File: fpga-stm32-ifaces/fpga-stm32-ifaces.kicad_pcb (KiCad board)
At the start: 6 copper layers, 90 x 94.5 mm, 274 parts, among them J1 0826-1G1T-23-F, J10 CORTEX_DEBUG_ETM, J11 XILINX_JTAG, J12 CONN_01X03, J2 PMOD_HOST, J3 PMOD_HOST, J4 XILINX_JTAG, J5 CONN_01X03, J6 CONN_01X03, J7 CONN_PCIE_PWR_8PIN, J8 XILINX_JTAG, J9 CONN_IBC_MGMT_DEVICE, M1 LOGO, M2 LOGO, M3 LOGO, M5 SCREWHOLE, M6 SCREWHOLE, M7 SCREWHOLE, M8 SCREWHOLE, U1 STM32H735-UFBGA176-25, U10 ECS-1612MV-250-CN, U11 STM32L431-QFN48, U12 MUN12AD03-SE, U13 MUN12AD03-SE, U14 MUN12AD03-SE, U15 MUN12AD03-SE, U16 W25Q128JV, U2 XC7S25-1FTGB196, U3 S25FL128SAGBHIA10, U4 KSZ9031RN, U5 RCLAMP0514M, U6 RCLAMP0514M, U7 ECS-1612MV-250-CN, U8 AT24MAC402, U9 ECS-1612MV-250-CN

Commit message: Lots of routing cleanup
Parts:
- moved R82 1.77 mm to (82.0, 131.0)
- moved R84 0.50 mm to (81.5, 126.8)
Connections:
- U2 pad B2: /MCU/FPGA_QSPI_DQ7 -> /MCU/FMC_NL_NADV
- U2 pad C1: /MCU/FMC_NL_NADV -> /MCU/FPGA_QSPI_DQ7
- U2 pad J3: /MCU/FMC_AD5 -> /MCU/RMII_RXD1
- U2 pad J4: /MCU/RMII_RXD1 -> /MCU/FMC_AD5
- U2 pad K3: /MCU/FMC_AD9 -> /MCU/RMII_RXD0
- U2 pad K4: /MCU/RMII_CRS_DV -> /MCU/FPGA_QSPI_DQS
- U2 pad L3: /MCU/FPGA_QSPI_DQS -> /MCU/FPGA_QSPI_DQ5
- U2 pad L5: /MCU/FPGA_QSPI_DQ5 -> /MCU/FPGA_QSPI_DQ4
- U2 pad M4: /MCU/RMII_RXD0 -> /MCU/RMII_CRS_DV
- U2 pad M5: /MCU/FPGA_QSPI_DQ4 -> /MCU/FMC_AD9
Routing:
- net /MCU/FMC_NBL1: track 44.1 -> 30.8 mm, vias 4 -> 2
- net /MCU/MCU_JTAG_TDI: track 69.4 -> 75.6 mm, vias 5 -> 4
- net /Power supply/1V0_EN: track 77.9 -> 71.9 mm
- net /MCU/FMC_NOE: track 29.6 -> 23.9 mm
- net /MCU/RMII_CRS_DV: track 31.8 -> 26.6 mm
- net /MCU/FPGA_QSPI_DQ3: track 41.8 -> 36.6 mm
- net /MCU/MCU_UART_RX: track 38.4 -> 33.5 mm
- net /MCU/FPGA_QSPI_DQ2: track 46.5 -> 41.7 mm
- net /Ethernet/ETH_RST_N: track 59.3 -> 63.9 mm, vias 2 -> 0
- net /MCU/RMII_REF_CLK: track 37.4 -> 32.9 mm
- net /MCU/FPGA_QSPI_DQ7: track 25.7 -> 21.4 mm, vias 3 -> 0
- net /MCU/MCU_UART_TX: track 36.0 -> 31.7 mm
- net /MCU/FPGA_QSPI_DQ6: track 21.7 -> 17.6 mm
- net /MCU/MCU_PMOD_DQ3: track 33.3 -> 30.3 mm, vias 3 -> 2
- net /MCU/FPGA_QSPI_DQ5: track 19.3 -> 16.4 mm
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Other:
- board text added: "FPGA-STM32H7 Interface Test A. Zonenberg / v0.1 / 2024-06-17"

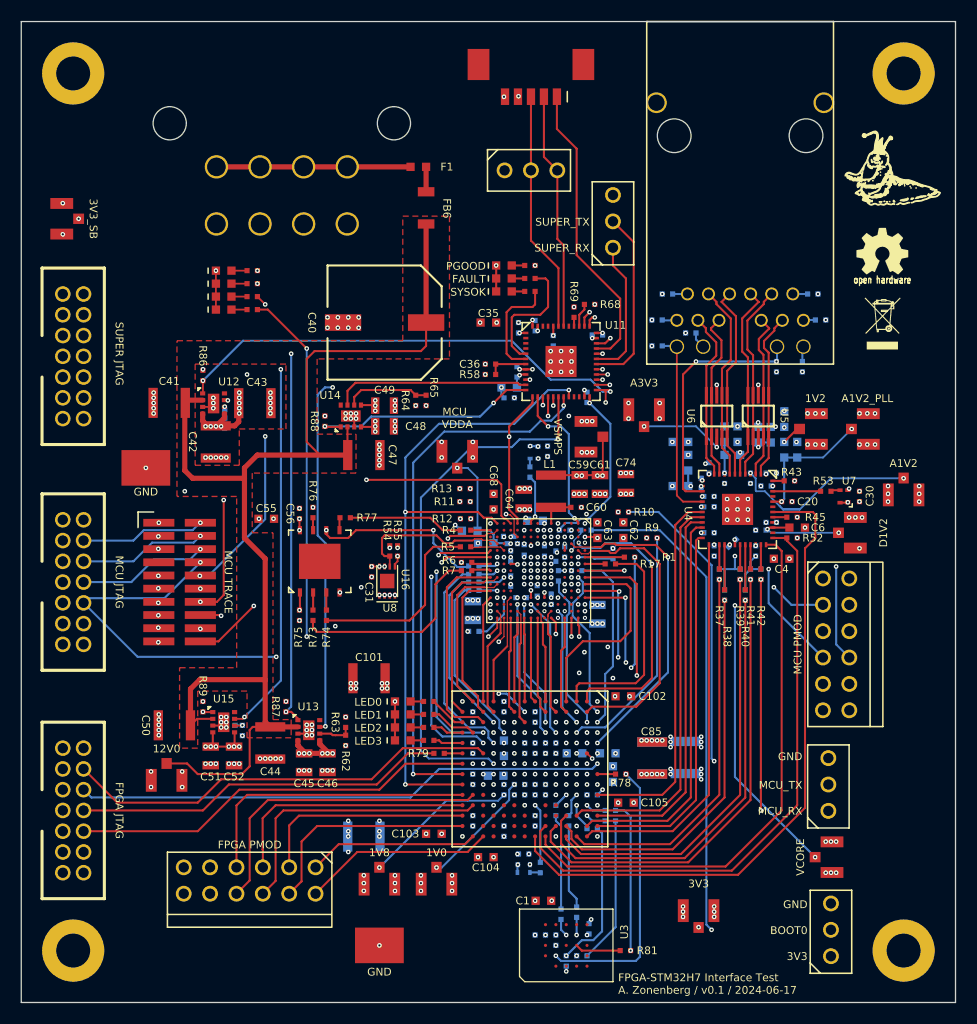
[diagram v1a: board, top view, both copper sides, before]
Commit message: More routing cleanup
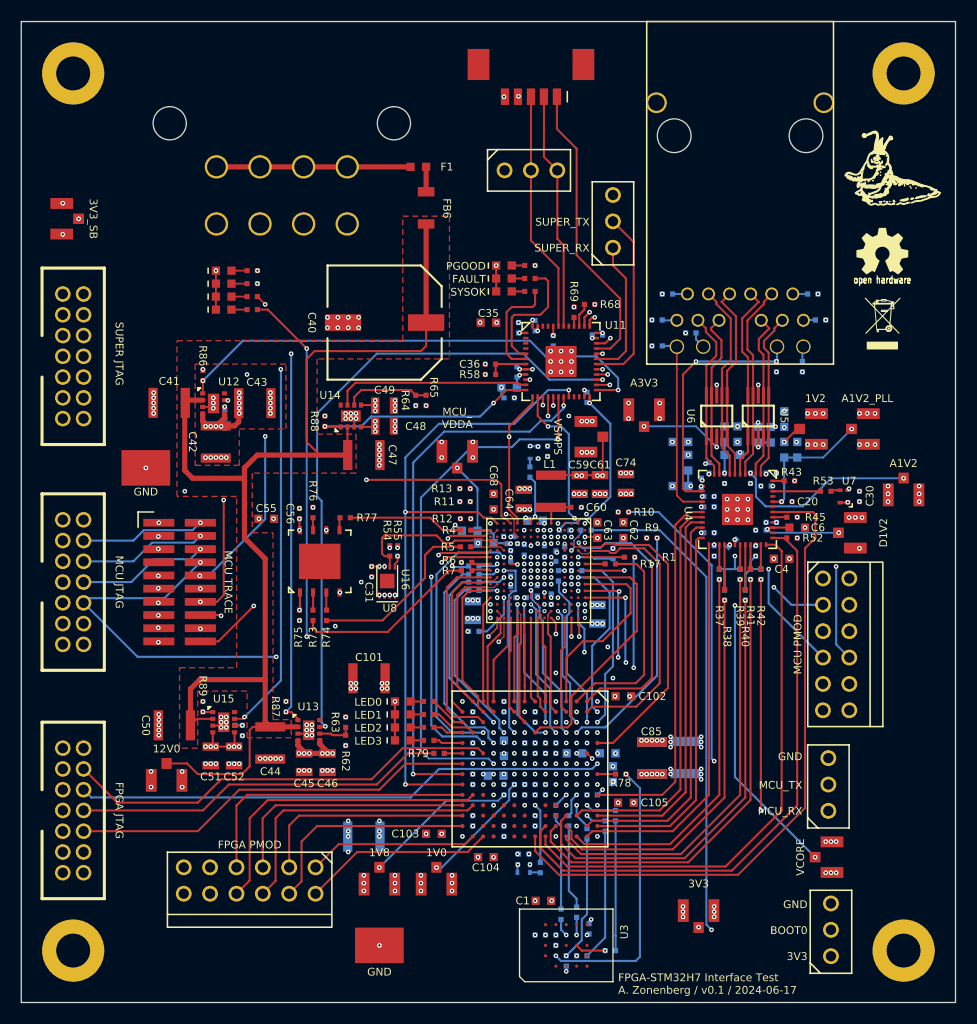
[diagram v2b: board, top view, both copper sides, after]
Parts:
- R81: moved to B.Cu
- moved R81 1.45 mm to (84.8, 130.5)
- moved R20 0.71 mm to (85.2, 117.5), turned to 90 degrees
- moved R21 0.71 mm to (84.2, 118.5), turned to 90 degrees
- moved R24 0.71 mm to (82.5, 119.2), turned to 90 degrees
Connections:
- U2 pad G4: /MCU/RMII_REF_CLK -> /MCU/FMC_CLK
- U2 pad H4: /MCU/FMC_CLK -> /MCU/RMII_REF_CLK
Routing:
- net /MCU/FMC_CLK: track 28.3 -> 25.2 mm, vias 2 -> 0
- net /MCU/FPGA_QSPI_SCK: track 24.9 -> 27.6 mm, vias 3 -> 2
- net /MCU/TRACED1: track 46.2 -> 43.7 mm
- net /Ethernet/FPGA_FLASH_CS_N: track 14.5 -> 12.1 mm
- net /Ethernet/FPGA_FLASH_DQ0: track 14.6 -> 12.5 mm, vias 1 -> 0
- net /Ethernet/A1V2: track 25.7 -> 23.7 mm
- net /MCU/MCU_FLASH_DQ1: track 19.5 -> 17.6 mm
- net /MCU/MCU_FLASH_DQ2: track 18.7 -> 17.1 mm
- net /MCU/MCU_FLASH_SCK: track 16.7 -> 15.2 mm
- net /MCU/FMC_NWE: track 14.5 -> 16.0 mm
- net /Ethernet/FPGA_FLASH_DQ1: track 14.1 -> 12.7 mm
- net Net-(U3-MOSI/DQ0): track 4.31 -> 2.96 mm, vias 0 -> 1
- net /MCU/MCU_PMOD_DQ3: track 30.3 -> 29.2 mm
- net /MCU/SUPER_SPI_SCK: track 21.6 -> 22.6 mm
- net Net-(U2C-IO_L1P_T0_D00_MOSI_14): track 1.96 -> 2.96 mm
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
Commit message: More routing cleanup
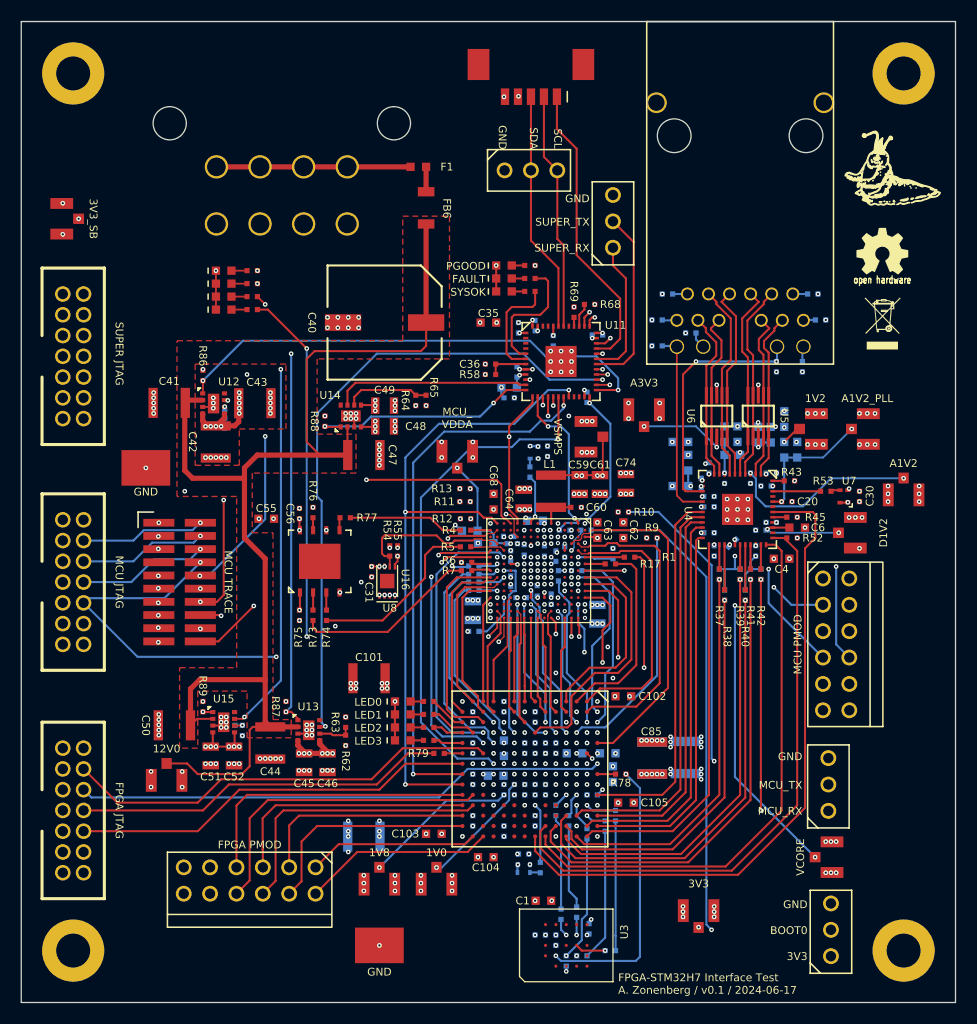
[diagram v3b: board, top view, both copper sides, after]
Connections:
- U2 pad B1: /MCU/FMC_NBL0 -> /MCU/FMC_NL_NADV
- U2 pad B2: /MCU/FMC_NL_NADV -> /MCU/FMC_NBL0
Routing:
- net /Power supply/1V8: track 66.5 -> 72.1 mm
- net /MCU/MCU_JTAG_TCK: track 71.5 -> 67.7 mm, vias 3 -> 2
- net /MCU/FMC_NBL0: track 26.5 -> 29.3 mm, vias 2 -> 0
- net /MCU/FMC_NL_NADV: track 28.6 -> 26.2 mm
- net /MCU/FMC_NBL1: track 31.3 -> 33.7 mm
- net /MCU/FPGA_QSPI_DQ7: track 20.6 -> 18.7 mm
- net /MCU/MCU_JTAG_TDO: track 72.6 -> 74.2 mm, vias 3 -> 2
- net /FPGA_RST_N: track 51.6 -> 49.9 mm
- net /MCU/FPGA_QSPI_DQ2: track 41.7 -> 40.4 mm
- net /Power support/VSMPS: track 42.8 -> 44.0 mm, vias 9 -> 8
- net /MCU/FPGA_QSPI_DQ3: track 36.6 -> 35.4 mm
- net /MCU/RMII_REF_CLK: track 31.9 -> 30.8 mm
- net /MCU/FMC_AD3: track 19.1 -> 18.3 mm
- net /Power supply/1V0: track 86.7 -> 87.5 mm
- net /MCU/MCU_JTAG_TDI: track 75.6 -> 75.0 mm, vias 4 -> 3
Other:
- board text added: "SCL"
- board text added: "SDA"

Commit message: More routing cleanup ready for layout review
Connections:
- U2 pad B3: /MCU/FPGA_QSPI_CS_N -> /MCU/FMC_AD2
- U2 pad C3: /MCU/FMC_NWAIT -> /MCU/FPGA_QSPI_CS_N
- U2 pad D3: /MCU/FMC_AD2 -> /MCU/FMC_NWAIT
- U2 pad M4: /MCU/RMII_CRS_DV -> /MCU/FMC_AD9
- U2 pad M5: /MCU/FMC_AD9 -> /MCU/RMII_CRS_DV
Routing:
- net /MCU/RMII_RXD1: track 16.1 -> 24.5 mm
- net /MCU/MCU_JTAG_TDI: track 75.0 -> 66.9 mm, vias 3 -> 2
- net /Power support/VCORE: track 69.0 -> 63.0 mm
- net /MCU/MCU_PMOD_DQ1: track 25.9 -> 30.8 mm, vias 2 -> 1
- net /Power supply/1V8: track 72.1 -> 67.9 mm
- net /MCU/FMC_NOE: track 24.3 -> 20.3 mm
- net /MCU/RMII_CRS_DV: track 26.4 -> 29.7 mm
- net /MCU/FPGA_QSPI_SCK: track 27.6 -> 29.6 mm
- net /MCU/FMC_AD9: track 27.2 -> 25.4 mm, vias 3 -> 2
- net /MCU_RST_N: track 53.5 -> 55.1 mm
- net /MCU/MCU_PMOD_DQ0: track 29.2 -> 28.1 mm
- net /MCU/SUPER_SPI_SCK: track 22.6 -> 21.6 mm
- net /MCU/MCU_PMOD_DQ4: track 32.2 -> 33.1 mm
- net /Power supply/SUPER_UART_TX: track 17.6 -> 16.7 mm
- net /MCU/FPGA_QSPI_DQ6: track 17.6 -> 18.4 mm
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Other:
- board text added: "FPGA-STM32H7 Interface Test A. Zonenberg / v0.1 / 2024-06-18"
- board text removed: "FPGA-STM32H7 Interface Test A. Zonenberg / v0.1 / 2024-06-17"

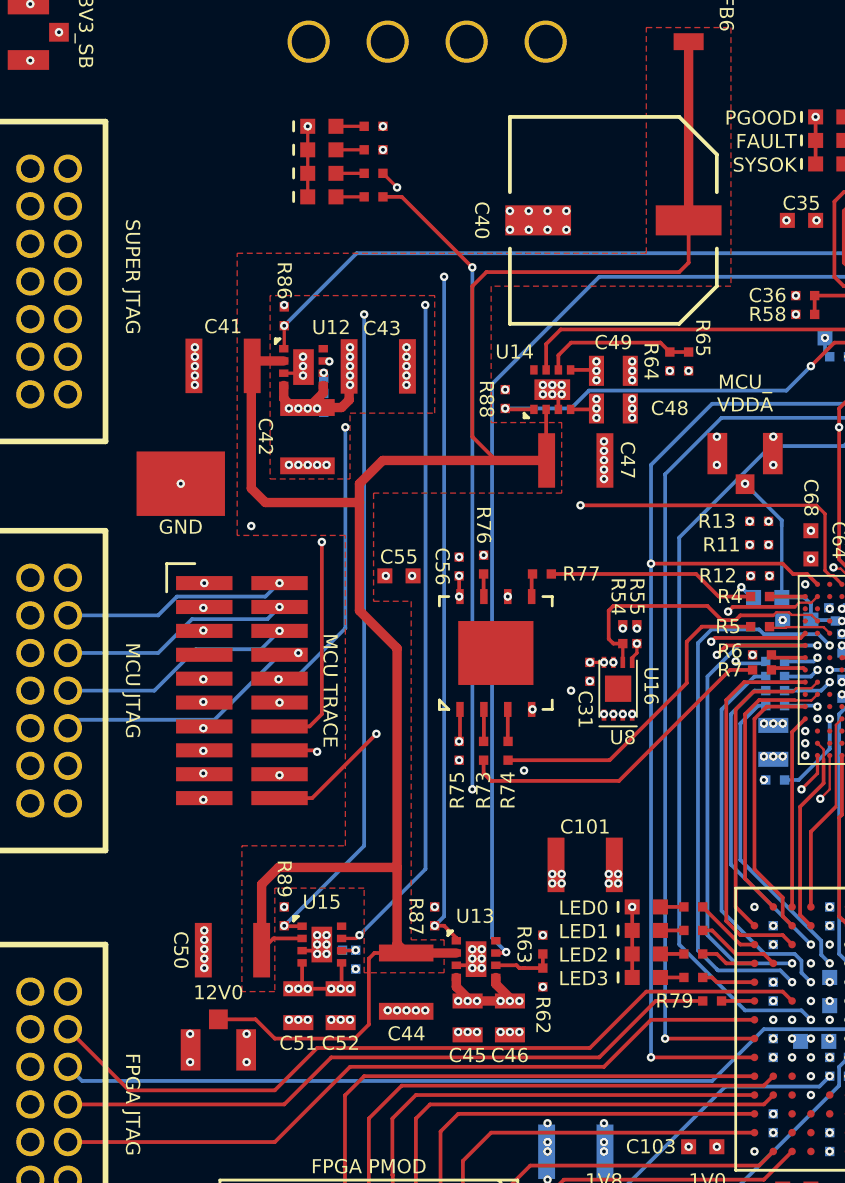
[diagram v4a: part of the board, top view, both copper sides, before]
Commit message: Finished interface test board, ready to order
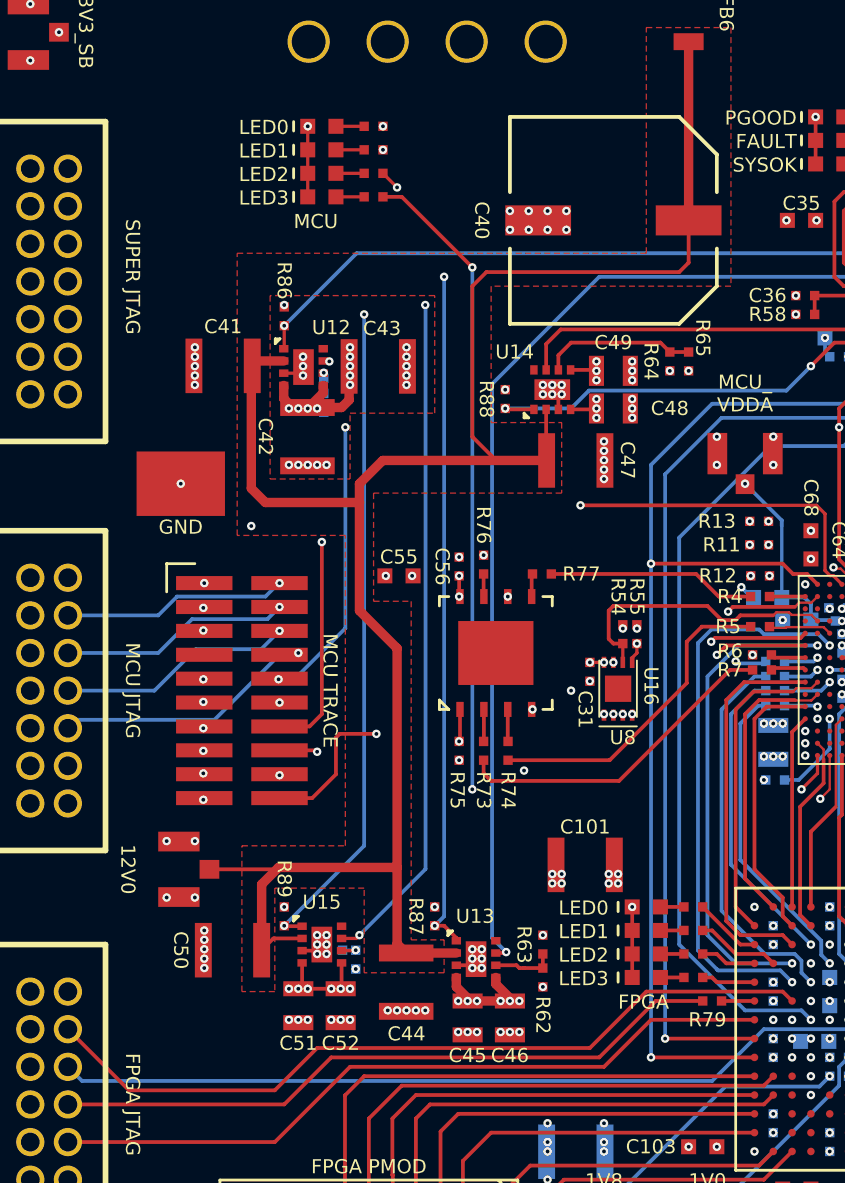
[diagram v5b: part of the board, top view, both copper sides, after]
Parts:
- moved TP6 9.71 mm to (40.0, 104.5), turned to 90 degrees
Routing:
- net /12V0: track 120.8 -> 110.5 mm
- net /GND: track 1077.2 -> 1085.6 mm
- net /MCU/TRACED3: track 49.8 -> 51.0 mm
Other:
- board text added: "FPGA"
- board text added: "MCU"
- board text added: "Place UL mark and date code in this area"
